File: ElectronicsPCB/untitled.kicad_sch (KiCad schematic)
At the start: 0 parts

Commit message: added rs232 port & stepdown for communication with teensy
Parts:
- added C1, C2, C3, C4: 0.1µF, symbol Device:C
- added J1: DE9_Socket_MountingHoles, Connector_Dsub:DSUB-9_Socket_Vertical_P2.77x2.84mm_MountingHoles, symbol Connector:DE9_Socket_MountingHoles
- added U1: max3323eepe+, 21-0043_P16+3_MXM, symbol VectorNav2:max3323eepe+
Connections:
- new net: C1.1, U1.1 (C1+)
- new net: C1.2, U1.3 (C1-)
- new net: J1.1, J1.4, J1.6
- new net: J1.7, J1.8
- new net: C4.2, U1.2 (V+)
- new net: C2.1, U1.4 (C2+)
- new net: C2.2, U1.5 (C2-)
- new net: C3.1, U1.6 (V-)
- new net +5V: U1.11 (TXENABLE), U1.12 (RENABLE), U1.13 (VL), U1.14 (*SHDN), U1.16 (VCC)
- new net GND: C3.2, C4.1, J1.5, U1.15 (GND)
- new net Teensy RX: U1.9 (ROUT1)
- new net Teensy TX: U1.10 (TIN1)
- new net VectorNav RX: J1.2, U1.7 (TOUT1)
- new net VectorNav TX: J1.3, U1.8 (RIN1)

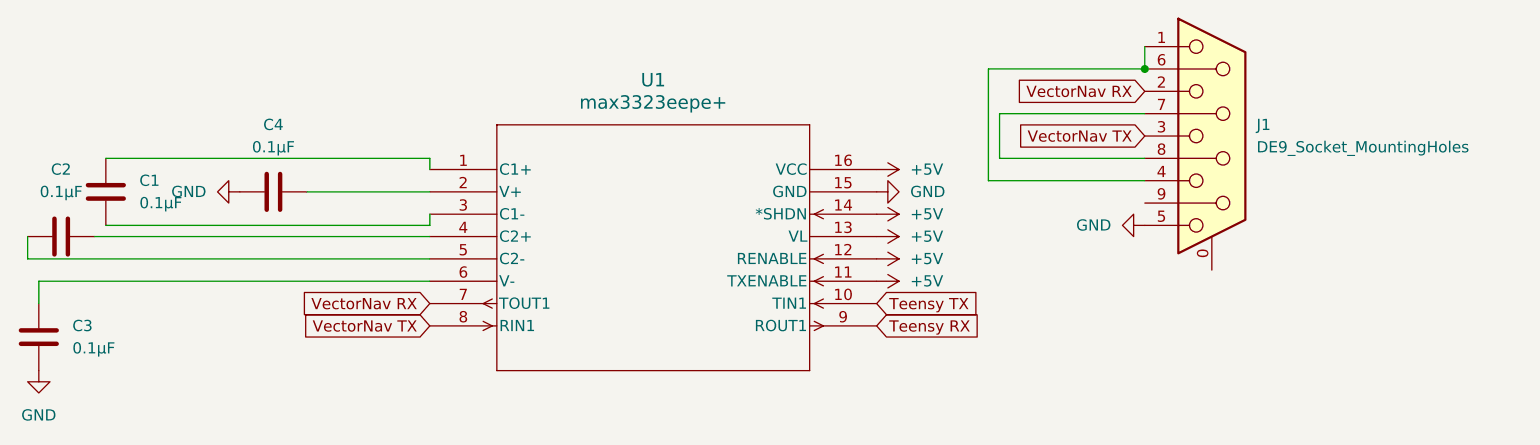
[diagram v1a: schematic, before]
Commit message: updated global label names for vectornav
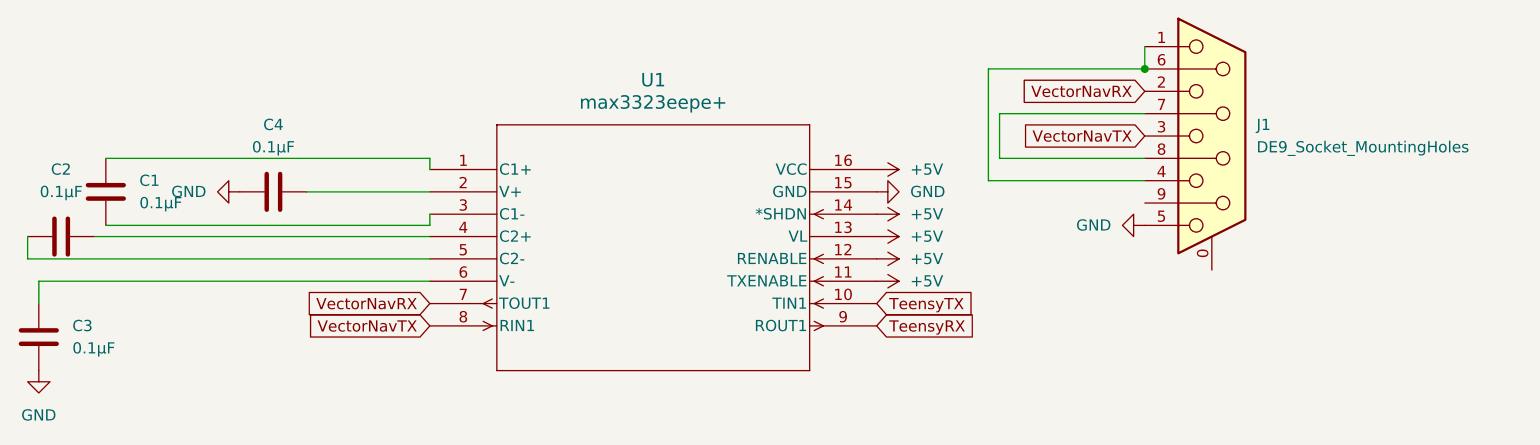
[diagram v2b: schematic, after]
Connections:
- net Teensy RX renamed TeensyRX
- net Teensy TX renamed TeensyTX
- net VectorNav RX renamed VectorNavRX
- net VectorNav TX renamed VectorNavTX
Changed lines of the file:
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@@
 		)
 	)
-	(global_label "VectorNav TX"
+	(global_label "VectorNavTX"
 		(shape input)
 		(at 87.63 127 180)
@@
 		)
 		(property "Intersheetrefs" "${INTERSHEET_REFS}"
-			(at 72.1263 127 0)
+			(at 73.0939 127 0)
 			(effects
 				(font
@@
 		)
 	)
-	(global_label "VectorNav RX"
+	(global_label "VectorNavRX"
 		(shape input)
 		(at 168.91 100.33 180)
@@
 		)
 		(property "Intersheetrefs" "${INTERSHEET_REFS}"
-			(at 153.1039 100.33 0)
+			(at 154.0715 100.33 0)
 			(effects
 				(font
@@
 		)
 	)
-	(global_label "Teensy RX"
+	(global_label "TeensyRX"
 		(shape input)
 		(at 138.43 127 0)
@@
 		)
 		(property "Intersheetrefs" "${INTERSHEET_REFS}"
-			(at 151.1518 127 0)
+			(at 150.1842 127 0)
 			(effects
 				(font
@@
 		)
 	)
-	(global_label "Teensy TX"
+	(global_label "TeensyTX"
 		(shape input)
 		(at 138.43 124.46 0)
@@
 		)
 		(property "Intersheetrefs" "${INTERSHEET_REFS}"
-			(at 150.8494 124.46 0)
+			(at 149.8818 124.46 0)
 			(effects
 				(font
@@
 		)
 	)
-	(global_label "VectorNav TX"
+	(global_label "VectorNavTX"
 		(shape input)
 		(at 168.91 105.41 180)
@@
 		)
 		(property "Intersheetrefs" "${INTERSHEET_REFS}"
-			(at 153.4063 105.41 0)
+			(at 154.3739 105.41 0)
 			(effects
 				(font
@@
 		)
 	)
-	(global_label "VectorNav RX"
+	(global_label "VectorNavRX"
 		(shape input)
 		(at 87.63 124.46 180)
@@
 		)
 		(property "Intersheetrefs" "${INTERSHEET_REFS}"
-			(at 71.8239 124.46 0)
+			(at 72.7915 124.46 0)
 			(effects
 				(font

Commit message: added Xbee and merged sheets
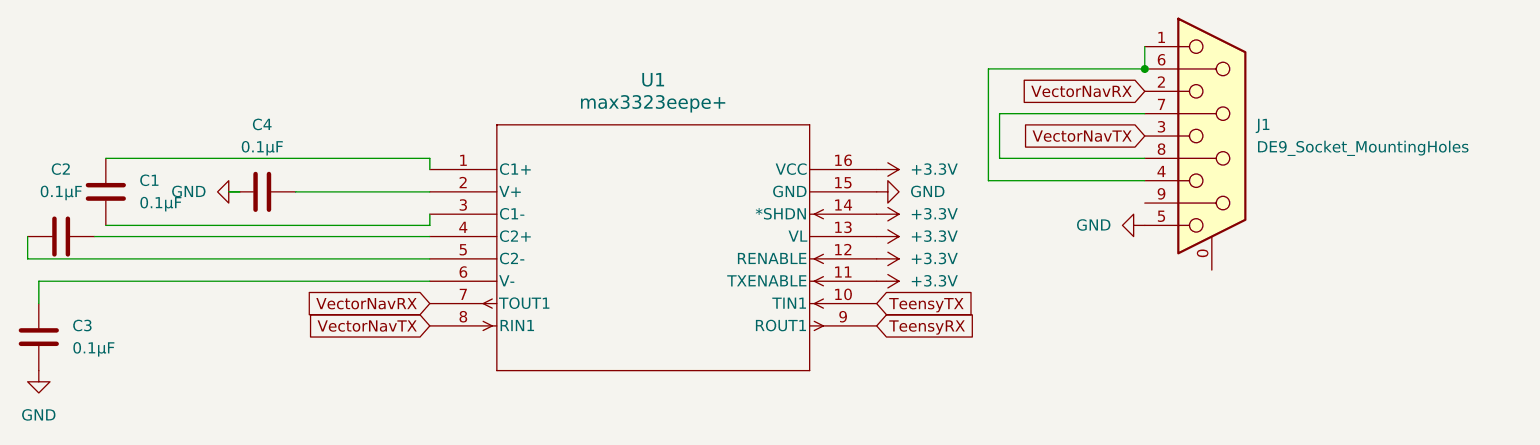
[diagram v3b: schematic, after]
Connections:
- net +5V renamed +3.3V
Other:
- moved on the sheet: C4
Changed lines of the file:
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@@
 	(wire
 		(pts
-			(xy 73.66 111.76) (xy 87.63 111.76)
+			(xy 72.39 111.76) (xy 87.63 111.76)
 		)
 		(stroke
@@
 		(pts
 			(xy 151.13 110.49) (xy 168.91 110.49)
+		)
+		(stroke
+			(width 0)
+			(type default)
+		)
+	)
+	(wire
+		(pts
+			(xy 64.77 111.76) (xy 66.04 111.76)
 		)
 		(stroke
@@
 	(symbol
 		(lib_id "Device:C")
-		(at 69.85 111.76 90)
+		(at 68.58 111.76 90)
 		(unit 1)
 		(exclude_from_sim no)
@@
 		(fields_autoplaced yes)
 		(property "Reference" "C4"
-			(at 69.85 104.14 90)
+			(at 68.58 104.14 90)
 			(effects
 				(font
@@
 		)
 		(property "Value" "0.1µF"
-			(at 69.85 106.68 90)
+			(at 68.58 106.68 90)
 			(effects
 				(font
@@
 		)
 		(property "Footprint" ""
-			(at 73.66 110.7948 0)
+			(at 72.39 110.7948 0)
 			(effects
 				(font
@@
 		)
 		(property "Datasheet" "~"
-			(at 69.85 111.76 0)
+			(at 68.58 111.76 0)
 			(effects
 				(font
@@
 		)
 		(property "Description" "Unpolarized capacitor"
-			(at 69.85 111.76 0)
+			(at 68.58 111.76 0)
 			(effects
 				(font
@@
 			)
 		)
-		(property "Value" "+5V"
+		(property "Value" "+3.3V"
 			(at 142.24 116.8399 90)
 			(effects
@@
 			)
 		)
-		(property "Value" "+5V"
+		(property "Value" "+3.3V"
 			(at 142.24 119.3799 90)
 			(effects
@@
 			)
 		)
-		(property "Value" "+5V"
+		(property "Value" "+3.3V"
 			(at 142.24 121.9199 90)
 			(effects
@@
 			)
 		)
-		(property "Value" "+5V"
+		(property "Value" "+3.3V"
 			(at 142.24 114.2999 90)
 			(effects
@@
 			)
 		)
-		(property "Value" "+5V"
+		(property "Value" "+3.3V"
 			(at 142.24 109.2199 90)
 			(effects
